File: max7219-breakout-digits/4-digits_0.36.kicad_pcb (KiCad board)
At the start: 2 copper layers, 47 x 15.5 mm, 6 parts, among them J1 Conn_02x08_Odd_Even, U1 HDSM-443B_7-Segment_2_Digit, U2 HDSM-443B_7-Segment_2_Digit

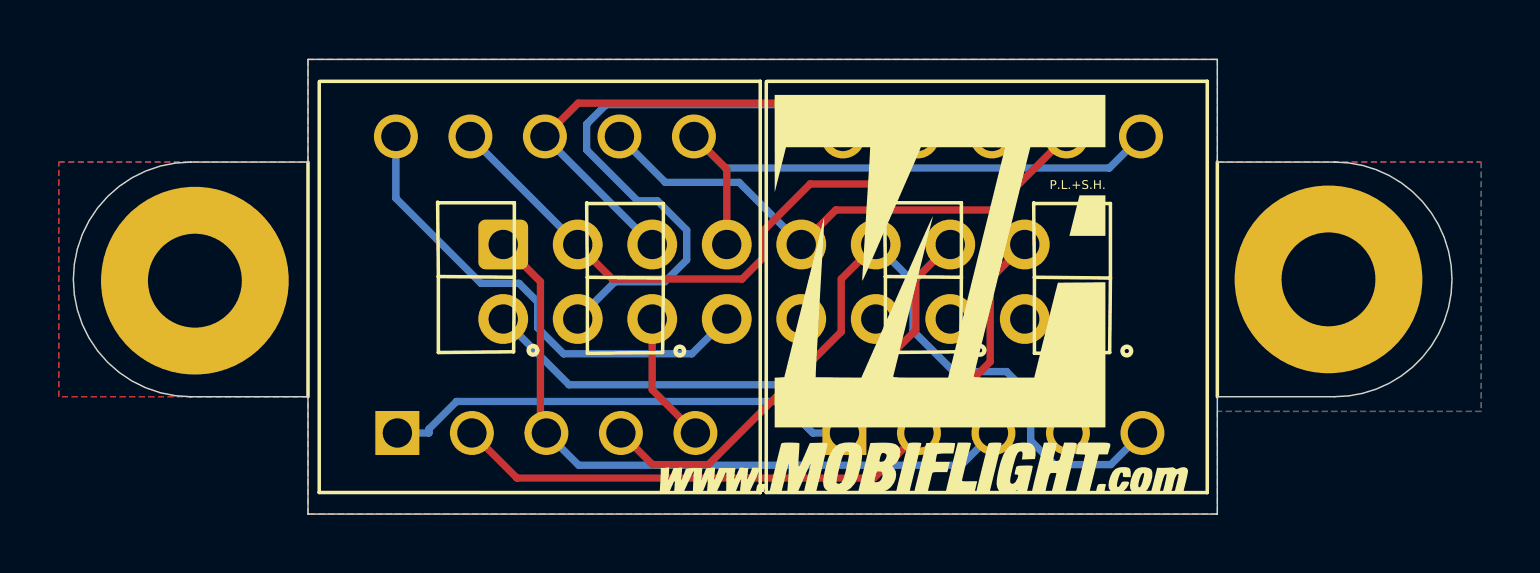
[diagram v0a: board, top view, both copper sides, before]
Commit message: center IDC on all 0.36 display boards
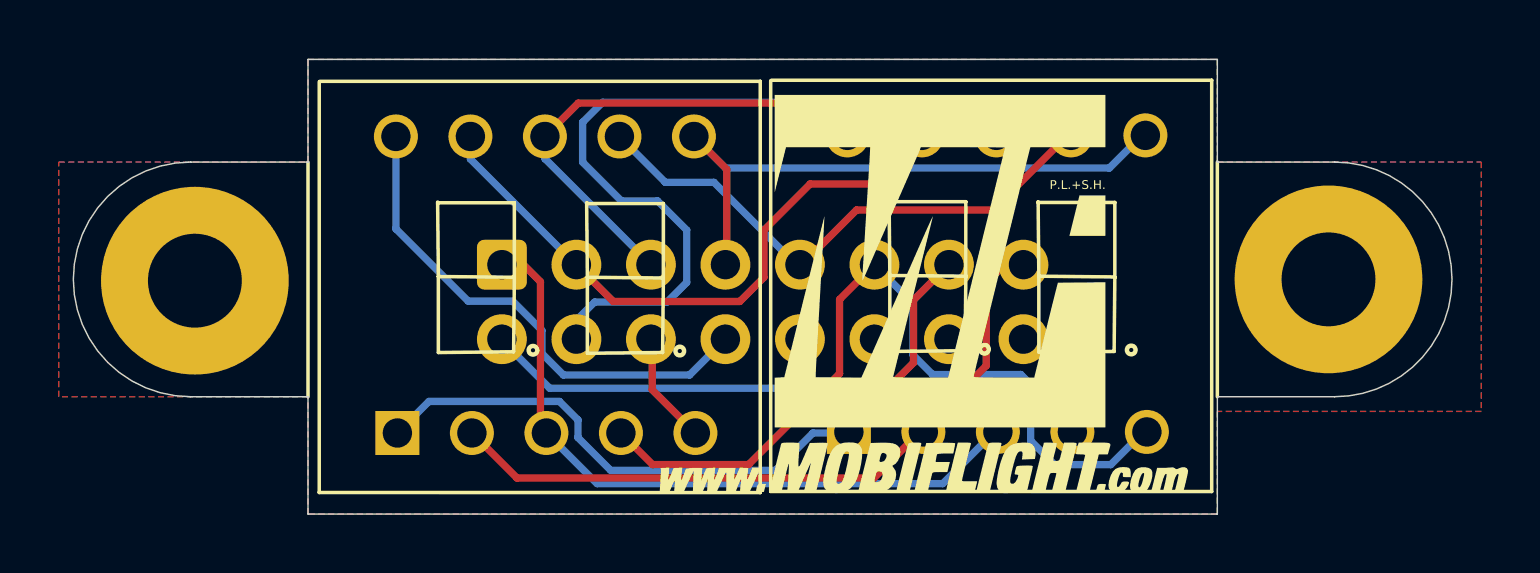
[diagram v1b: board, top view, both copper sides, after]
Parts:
- moved J1 0.69 mm to (86.3, 58.3)
- moved U2 0.16 mm to (107.1, 58.9)
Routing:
- net /B: track 19.8 -> 21.2 mm
- net /DIG1: track 20.4 -> 21.5 mm
- net /DIG3: track 16.6 -> 17.4 mm
- net /D: track 20.3 -> 21.0 mm
- net /C: track 21.4 -> 22.0 mm
- net /G: track 24.1 -> 24.8 mm
- net /E: track 18.3 -> 18.9 mm
- net /A: track 23.2 -> 23.7 mm
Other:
- board text added: "MobiFlight Display System 4 Digits ${REVISION}"
- board text removed: "4 Digit Module ${REVISION}"

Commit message: add additional labels on front on backside from all boards
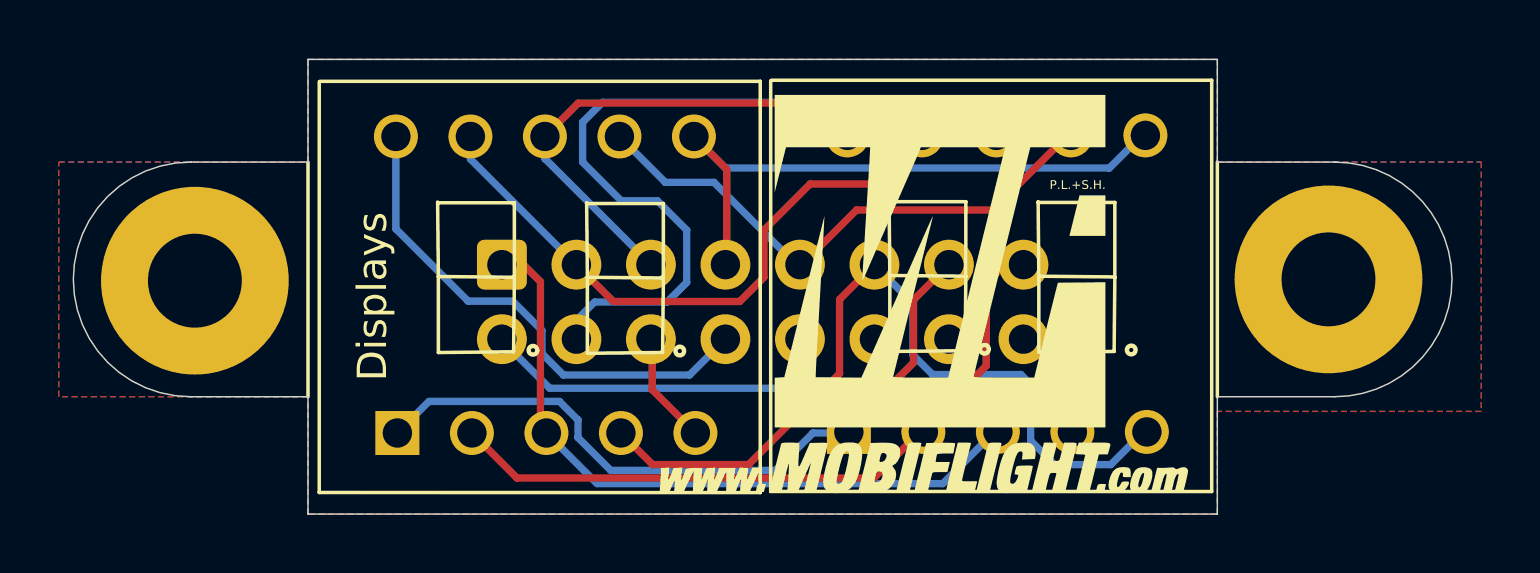
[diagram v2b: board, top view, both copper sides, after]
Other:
- board text added: "Displays"
- board text added: "IDC"
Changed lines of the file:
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@@
 		(layer "Edge.Cuts")
+	)
+	(gr_text "Displays"
+		(at 82.5 62.317839 90)
+		(layer "F.SilkS" knockout)
+		(effects
+			(font
+				(size 1 1)
+				(thickness 0.15)
+			)
+			(justify left bottom)
+		)
 	)
 	(gr_text "P.L.+S.H."
@@
 		)
 	)
+	(gr_text "IDC"
+		(at 85.17 56.44641 90)
+		(layer "B.SilkS" knockout)
+		(effects
+			(font
+				(size 2 2)
+				(thickness 0.25)
+			)
+			(justify left bottom mirror)
+		)
+	)

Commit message: center all IDC connectors on 0.36 boards, move displays closer together
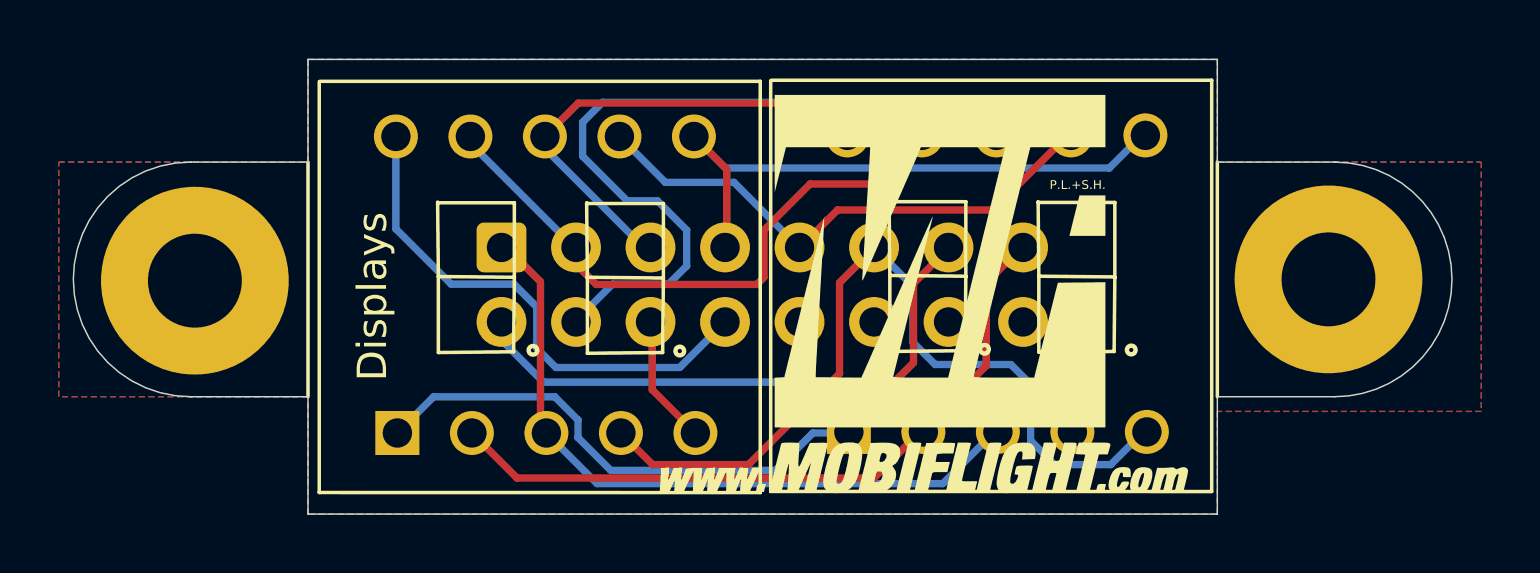
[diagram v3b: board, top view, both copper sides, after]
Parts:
- moved J1 0.59 mm to (86.3, 57.8)
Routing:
- net /DIG0: track 24.8 -> 26.0 mm
- net /F: track 23.6 -> 24.5 mm
- net /G: track 24.8 -> 25.5 mm
